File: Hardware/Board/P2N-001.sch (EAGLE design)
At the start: 35 parts, among them IC1 4053N, IC2 LTC485N, IC3 74LS07N, IC4 LTC485N, K1 G5V1, T1 2SC1815

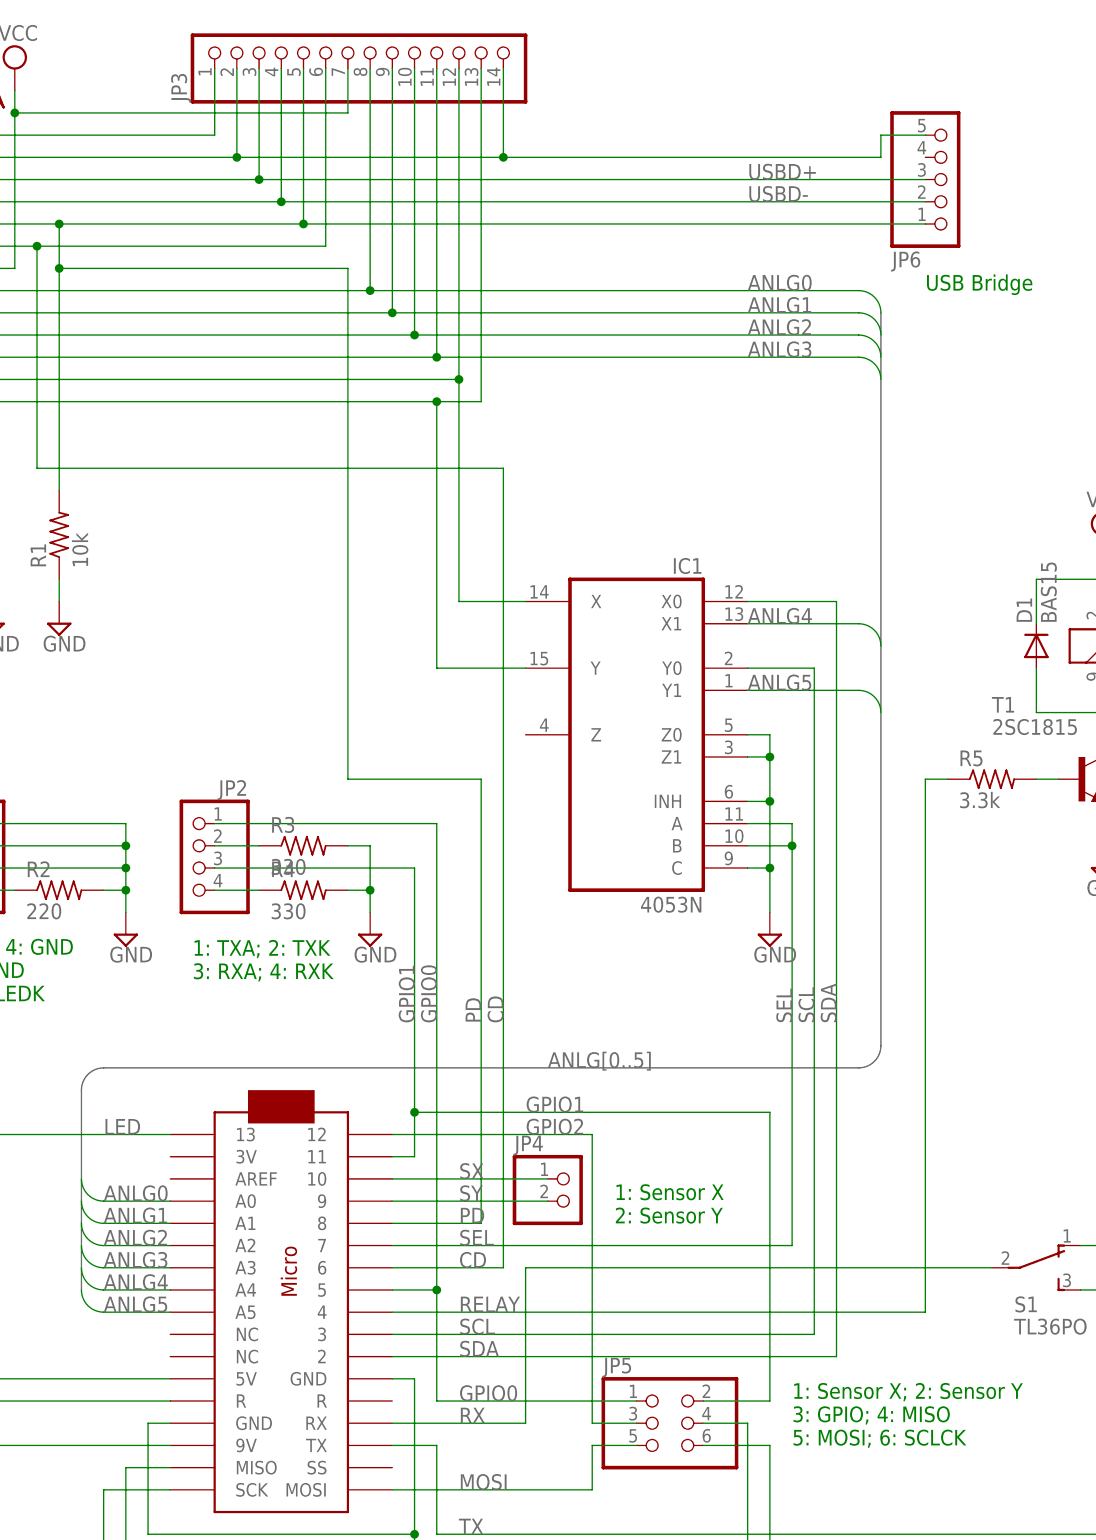
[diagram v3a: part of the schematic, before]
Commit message: Added anther LED pattern.
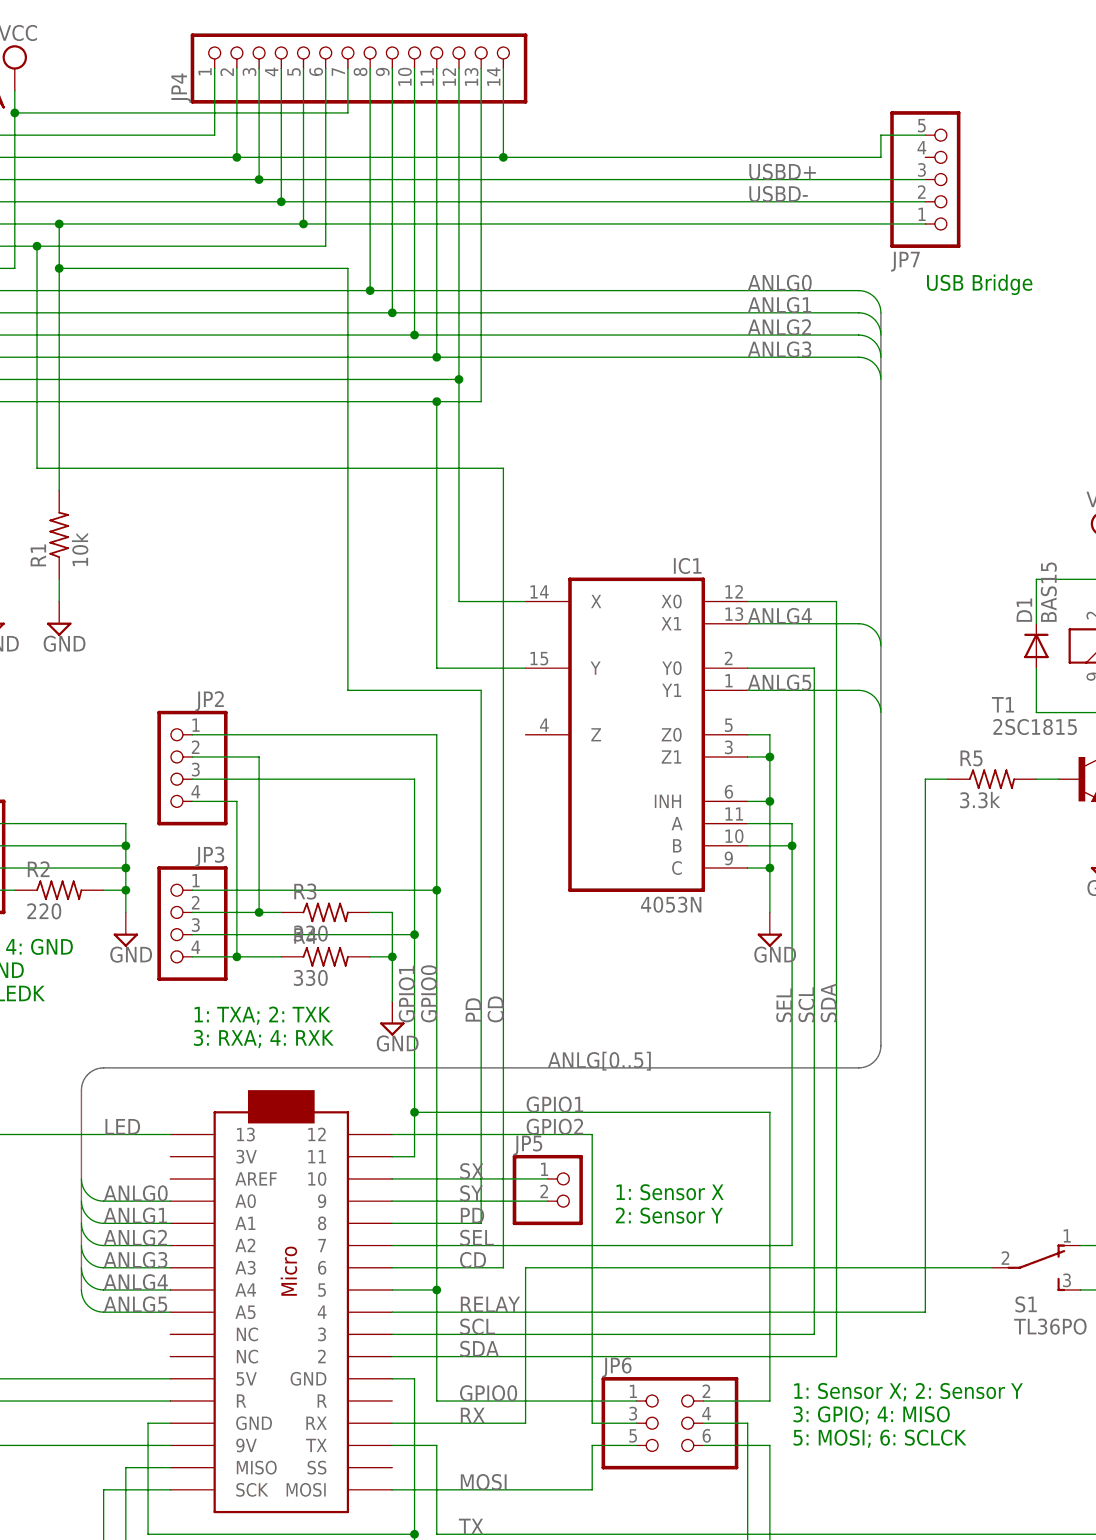
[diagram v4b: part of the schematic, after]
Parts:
- added JP7: (no value), pinhead:PINHD-1X5/90
- JP3: device pinhead:PINHD-1X14 -> pinhead:PINHD-1X4
- JP4: device pinhead:PINHD-1X2 -> pinhead:PINHD-1X14
- JP5: device pinhead:PINHD-2X3 -> pinhead:PINHD-1X2
- JP6: device pinhead:PINHD-1X5/90 -> pinhead:PINHD-2X3
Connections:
- net ANLG0: now also JP4.8; no longer JP3.8
- net ANLG1: now also JP4.9; no longer JP3.9
- net ANLG2: now also JP4.10; no longer JP3.10
- net ANLG3: now also JP4.11; no longer JP3.11
- net CD: now also JP4.6; no longer JP3.6
- net GND: now also JP4.14, JP4.2, JP7.5; no longer JP3.14, JP3.2, JP6.5
- net GPIO0: now also JP3.1, JP6.1; no longer JP5.1
- net GPIO1: now also JP3.3, JP6.2; no longer JP5.2
- net GPIO2: now also JP6.3; no longer JP5.3
- net MISO: now also JP6.4; no longer JP5.4
- net MOSI: now also JP6.5; no longer JP5.5
- net N$17: now also JP3.2
- net N$18: now also JP3.4
- net N$28: now also JP4.12; no longer JP3.12
- net N$29: now also JP4.13; no longer JP3.13
- net PD: now also JP4.5, JP7.1; no longer JP3.5, JP6.1
- net SCLK: now also JP6.6; no longer JP5.6
- net SX: now also JP5.1; no longer JP4.1
- net SY: now also JP5.2; no longer JP4.2
- net USBD+: now also JP4.3, JP7.3; no longer JP3.3, JP6.3
- net USBD-: now also JP4.4, JP7.2; no longer JP3.4, JP6.2
- net VCC: now also JP4.7; no longer JP3.7
- net VDD: now also JP4.1; no longer JP3.1
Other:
- moved on the sheet: JP2, R3, R4

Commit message: Removed LED jumper.
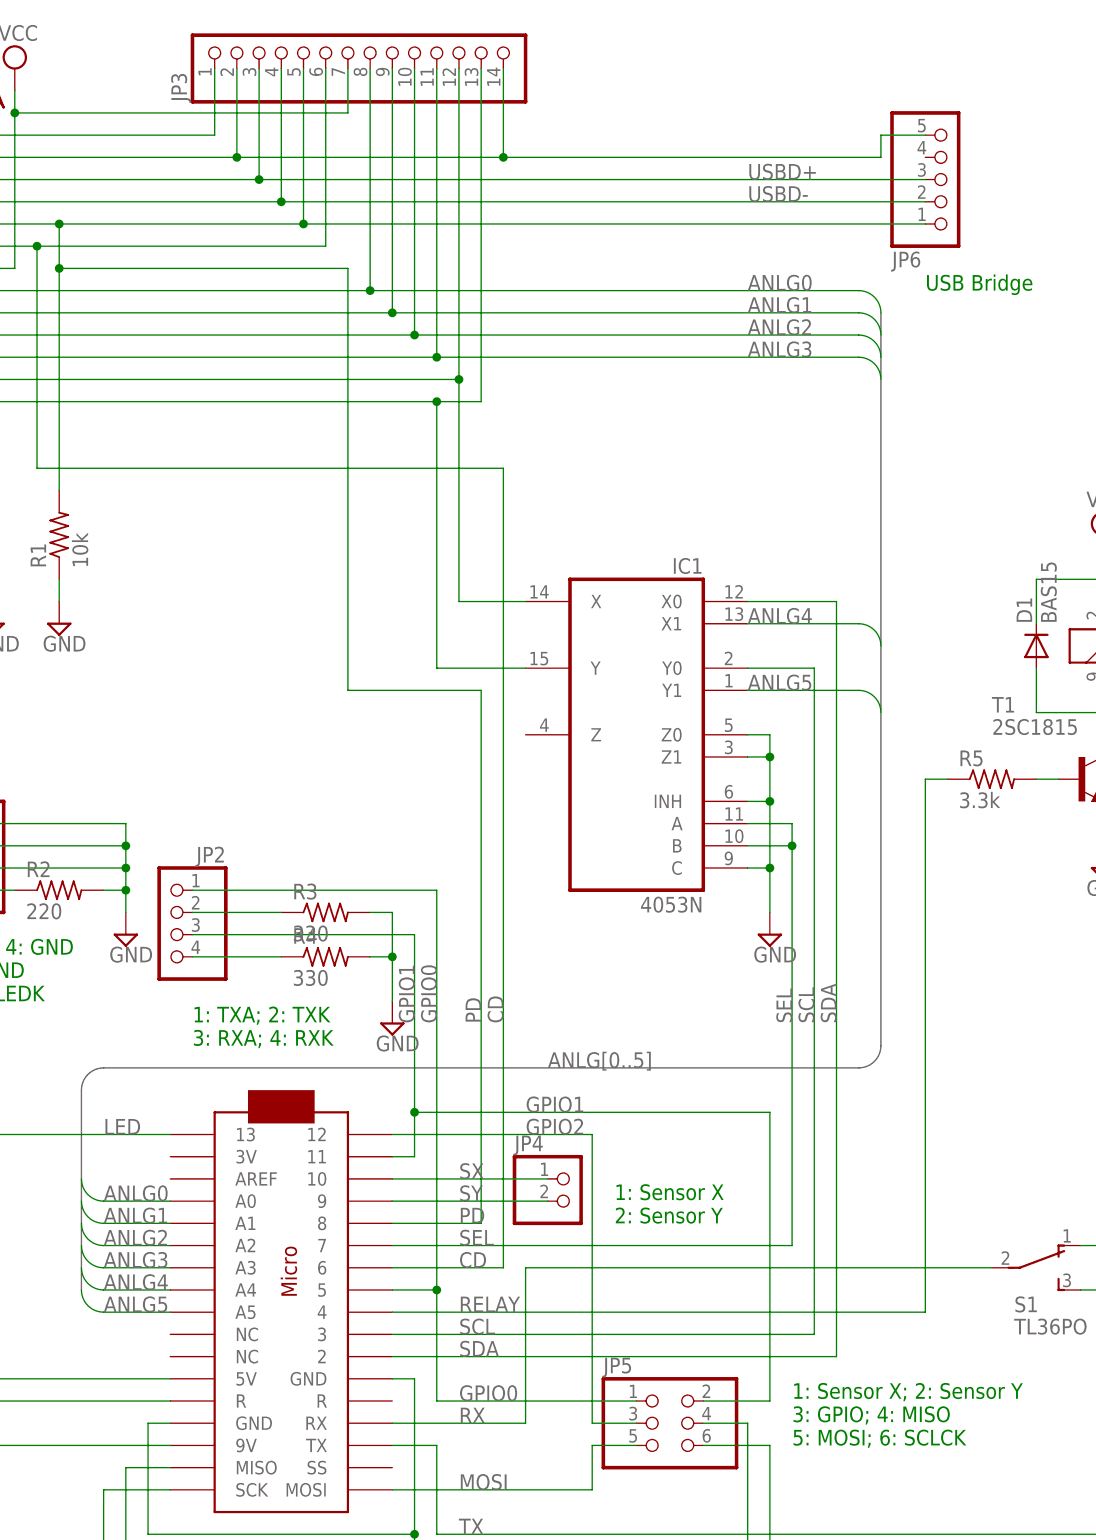
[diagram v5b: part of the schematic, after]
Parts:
- removed JP7: (no value), pinhead:PINHD-1X5/90
- JP3: device pinhead:PINHD-1X4 -> pinhead:PINHD-1X14
- JP4: device pinhead:PINHD-1X14 -> pinhead:PINHD-1X2
- JP5: device pinhead:PINHD-1X2 -> pinhead:PINHD-2X3
- JP6: device pinhead:PINHD-2X3 -> pinhead:PINHD-1X5/90
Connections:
- net ANLG0: now also JP3.8; no longer JP4.8
- net ANLG1: now also JP3.9; no longer JP4.9
- net ANLG2: now also JP3.10; no longer JP4.10
- net ANLG3: now also JP3.11; no longer JP4.11
- net CD: now also JP3.6; no longer JP4.6
- net GND: now also JP3.14, JP3.2, JP6.5; no longer JP4.14, JP4.2, JP7.5
- net GPIO0: now also JP5.1; no longer JP3.1, JP6.1
- net GPIO1: now also JP5.2; no longer JP3.3, JP6.2
- net GPIO2: now also JP5.3; no longer JP6.3
- net MISO: now also JP5.4; no longer JP6.4
- net MOSI: now also JP5.5; no longer JP6.5
- net N$17: no longer JP3.2
- net N$18: no longer JP3.4
- net N$28: now also JP3.12; no longer JP4.12
- net N$29: now also JP3.13; no longer JP4.13
- net PD: now also JP3.5, JP6.1; no longer JP4.5, JP7.1
- net SCLK: now also JP5.6; no longer JP6.6
- net SX: now also JP4.1; no longer JP5.1
- net SY: now also JP4.2; no longer JP5.2
- net USBD+: now also JP3.3, JP6.3; no longer JP4.3, JP7.3
- net USBD-: now also JP3.4, JP6.2; no longer JP4.4, JP7.2
- net VCC: now also JP3.7; no longer JP4.7
- net VDD: now also JP3.1; no longer JP4.1
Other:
- moved on the sheet: JP2
